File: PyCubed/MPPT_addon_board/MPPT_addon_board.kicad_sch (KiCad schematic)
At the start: 14 parts, among them J1 HW-09-08-L-D-285-SM-A, Q9 MBT2222ADW1T1, U1 LT8490-mezzanine, U2 LT8490-mezzanine

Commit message: adding version, name, and text on circuit board
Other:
- title: (none) -> MPPT addon board
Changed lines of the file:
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@@
 (kicad_sch (version 20230121) (generator eeschema)
   (paper "A4")
+  (title_block
+    (title "MPPT addon board")
+    (date "2024-05-07")
+    (rev "1.4")
+  )
   (junction (at 237.49 113.03) (diameter 0) (color 0 0 0 0)
   )

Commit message: finalized edits
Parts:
- added R29, R30: 10K, Resistor_SMD:R_0603_1608Metric, symbol Device:R_US
- C5, C6: value 0.1u -> 0.1uF
- U1, U2: value LT8490-mezzanine -> LT8491-mezzanine; footprint mainboard:LT8490-mezzanine -> mainboard:LT8491-mezzanine
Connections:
- net I2C Bus Protection/SDA_DEVICE: now also U1.12 (SDA); no longer U1.13 (SDA)
- net I2C Bus Protection/SDL_DEVICE: now also U1.13 (SCL); no longer U1.12 (SCL)
- net I2C Bus Protection1/SDA_DEVICE: now also U2.12 (SDA); no longer U2.13 (SDA)
- net I2C Bus Protection1/SDL_DEVICE: now also U2.13 (SCL); no longer U2.12 (SCL)
- net ~{SHDN_1}: now also R29.1; no longer Q9.5 (B2)
- net ~{SHDN_2}: now also R30.1; no longer Q9.2 (B1)
- new net: Q9.2 (B1), R30.2
- new net: Q9.5 (B2), R29.2
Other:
- note added: "Connector"
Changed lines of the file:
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@@
   (junction (at 92.71 41.91) (diameter 0) (color 0 0 0 0)
   )
+  (junction (at 224.79 58.42) (diameter 0) (color 0 0 0 0)
+  )
   (junction (at 118.11 139.7) (diameter 0) (color 0 0 0 0)
   )
@@
   (junction (at 118.11 129.54) (diameter 0) (color 0 0 0 0)
   )
+  (junction (at 207.01 128.27) (diameter 0) (color 0 0 0 0)
+  )
   (junction (at 92.71 72.39) (diameter 0) (color 0 0 0 0)
   )
@@
   )
   (junction (at 49.53 166.37) (diameter 0) (color 0 0 0 0)
+  )
+  (junction (at 238.76 58.42) (diameter 0) (color 0 0 0 0)
   )
   (no_connect (at 95.25 49.53))
@@
     (stroke (width 0) (type default))
   )
-  (wire (pts (xy 54.61 118.11) (xy 63.5 118.11))
+  (wire (pts (xy 45.72 118.11) (xy 55.88 118.11))
     (stroke (width 0) (type default))
   )
@@
     (stroke (width 0) (type default))
   )
+  (wire (pts (xy 44.45 57.15) (xy 58.42 57.15))
+    (stroke (width 0) (type default))
+  )
   (wire (pts (xy 115.57 111.76) (xy 129.54 111.76))
     (stroke (width 0) (type default))
@@
   )
   (wire (pts (xy 204.47 118.11) (xy 209.55 118.11))
-    (stroke (width 0) (type default))
-  )
-  (wire (pts (xy 55.88 57.15) (xy 66.04 57.15))
     (stroke (width 0) (type default))
   )
@@
     )
   )
+  (text "Connector\n" (at 214.63 95.25 0)
+    (effects (font (size 2.159 2.159)) (justify left bottom))
+  )
   (text "Local decoupling capasitors" (at 218.44 49.53 0)
     (effects (font (size 1.27 1.27)) (justify left bottom))
@@
     (effects (font (size 1.27 1.27)) (justify left bottom))
   )
-  (label "~{SHDN_1}" (at 55.88 57.15 0) (fields_autoplaced)
+  (label "~{SHDN_1}" (at 44.45 57.15 0) (fields_autoplaced)
     (effects (font (size 1.27 1.27)) (justify left bottom))
   )
@@
     (effects (font (size 1.27 1.27)) (justify right bottom))
   )
-  (label "~{SHDN_2}" (at 54.61 118.11 0) (fields_autoplaced)
+  (label "~{SHDN_2}" (at 45.72 118.11 0) (fields_autoplaced)
     (effects (font (size 1.27 1.27)) (justify left bottom))
   )
@@
     )
   )
+  (symbol (lib_id "power:PWR_FLAG") (at 207.01 128.27 90) (unit 1)
+    (in_bom yes) (on_board yes) (dnp no) (fields_autoplaced)
+    (property "Reference" "#FLG04" (at 205.105 128.27 0)
+      (effects (font (size 1.27 1.27)) hide)
+    )
+    (property "Value" "PWR_FLAG" (at 203.2 128.27 90)
+      (effects (font (size 1.27 1.27)) (justify left))
+    )
+    (property "Footprint" "" (at 207.01 128.27 0)
+      (effects (font (size 1.27 1.27)) hide)
+    )
+    (property "Datasheet" "~" (at 207.01 128.27 0)
+      (effects (font (size 1.27 1.27)) hide)
+    )
+    (pin "1")
+    (instances
+      (project "MPPT_addon_board"
+        (path "/280ad1e7-2eb5-41ea-be76-321f07a5cb3e"
+          (reference "#FLG04") (unit 1)
+        )
+      )
+    )
+  )
   (symbol (lib_id "Device:C") (at 224.79 64.77 0) (unit 1)
     (in_bom yes) (on_board yes) (dnp no) (fields_autoplaced)
@@
       (effects (font (size 1.27 1.27)) (justify left))
     )
-    (property "Value" "0.1u" (at 228.6 66.04 0)
+    (property "Value" "0.1uF" (at 228.6 66.04 0)
       (effects (font (size 1.27 1.27)) (justify left))
     )
@@
         (path "/280ad1e7-2eb5-41ea-be76-321f07a5cb3e"
           (reference "Q9") (unit 1)
+        )
+      )
+    )
+  )
+  (symbol (lib_id "power:PWR_FLAG") (at 238.76 58.42 270) (unit 1)
+    (in_bom yes) (on_board yes) (dnp no) (fields_autoplaced)
+    (property "Reference" "#FLG02" (at 240.665 58.42 0)
+      (effects (font (size 1.27 1.27)) hide)
+    )
+    (property "Value" "PWR_FLAG" (at 242.57 58.42 90)
+      (effects (font (size 1.27 1.27)) (justify left))
+    )
+    (property "Footprint" "" (at 238.76 58.42 0)
+      (effects (font (size 1.27 1.27)) hide)
+    )
+    (property "Datasheet" "~" (at 238.76 58.42 0)
+      (effects (font (size 1.27 1.27)) hide)
+    )
+    (pin "1")
+    (instances
+      (project "MPPT_addon_board"
+        (path "/280ad1e7-2eb5-41ea-be76-321f07a5cb3e"
+          (reference "#FLG02") (unit 1)
         )
       )
@@
       (effects (font (size 1.27 1.27)) (justify left))
     )
-    (property "Value" "0.1u" (at 242.57 66.04 0)
+    (property "Value" "0.1uF" (at 242.57 66.04 0)
       (effects (font (size 1.27 1.27)) (justify left))
     )
@@
       (effects (font (size 1.27 1.27)))
     )
-    (property "Value" "LT8490-mezzanine" (at 105.41 97.79 0)
-      (effects (font (size 1.27 1.27)))
-    )
-    (property "Footprint" "mainboard:LT8490-mezzanine" (at 100.33 97.79 0)
+    (property "Value" "LT8491-mezzanine" (at 105.41 97.79 0)
+      (effects (font (size 1.27 1.27)))
+    )
+    (property "Footprint" "mainboard:LT8491-mezzanine" (at 100.33 97.79 0)
       (effects (font (size 1.27 1.27)) hide)
     )
@@
     )
   )
+  (symbol (lib_id "power:PWR_FLAG") (at 224.79 58.42 90) (unit 1)
+    (in_bom yes) (on_board yes) (dnp no) (fields_autoplaced)
+    (property "Reference" "#FLG01" (at 222.885 58.42 0)
+      (effects (font (size 1.27 1.27)) hide)
+    )
+    (property "Value" "PWR_FLAG" (at 220.98 58.42 90)
+      (effects (font (size 1.27 1.27)) (justify left))
+    )
+    (property "Footprint" "" (at 224.79 58.42 0)
+      (effects (font (size 1.27 1.27)) hide)
+    )
+    (property "Datasheet" "~" (at 224.79 58.42 0)
+      (effects (font (size 1.27 1.27)) hide)
+    )
+    (pin "1")
+    (instances
+      (project "MPPT_addon_board"
+        (path "/280ad1e7-2eb5-41ea-be76-321f07a5cb3e"
+          (reference "#FLG01") (unit 1)
+        )
+      )
+    )
+  )
   (symbol (lib_id "power:GND") (at 92.71 142.24 0) (unit 1)
     (in_bom yes) (on_board yes) (dnp no) (fields_autoplaced)
@@
     )
   )
+  (symbol (lib_id "power:PWR_FLAG") (at 193.04 107.95 90) (unit 1)
+    (in_bom yes) (on_board yes) (dnp no) (fields_autoplaced)
+    (property "Reference" "#FLG03" (at 191.135 107.95 0)
+      (effects (font (size 1.27 1.27)) hide)
+    )
+    (property "Value" "PWR_FLAG" (at 189.23 107.95 90)
+      (effects (font (size 1.27 1.27)) (justify left))
+    )
+    (property "Footprint" "" (at 193.04 107.95 0)
+      (effects (font (size 1.27 1.27)) hide)
+    )
+    (property "Datasheet" "~" (at 193.04 107.95 0)
+      (effects (font (size 1.27 1.27)) hide)
+    )
+    (pin "1")
+    (instances
+      (project "MPPT_addon_board"
+        (path "/280ad1e7-2eb5-41ea-be76-321f07a5cb3e"
+          (reference "#FLG03") (unit 1)
+        )
+      )
+    )
+  )
+  (symbol (lib_id "Device:R_US") (at 59.69 118.11 90) (unit 1)
+    (in_bom yes) (on_board yes) (dnp no) (fields_autoplaced)
+    (property "Reference" "R30" (at 59.69 111.76 90)
+      (effects (font (size 1.27 1.27)))
+    )
+    (property "Value" "10K" (at 59.69 114.3 90)
+      (effects (font (size 1.27 1.27)))
+    )
+    (property "Footprint" "Resistor_SMD:R_0603_1608Metric" (at 59.944 117.094 90)
+      (effects (font (size 1.27 1.27)) hide)
+    )
+    (property "Datasheet" "~" (at 59.69 118.11 0)
+      (effects (font (size 1.27 1.27)) hide)
+    )
+    (property "note" "" (at 59.69 118.11 90)
+      (effects (font (size 1.27 1.27)) hide)
+    )
+    (pin "1")
+    (pin "2")
+    (instances
+      (project "MPPT_addon_board"
+        (path "/280ad1e7-2eb5-41ea-be76-321f07a5cb3e"
+          (reference "R30") (unit 1)
+        )
+      )
+    )
+  )
   (symbol (lib_id "power:GND") (at 238.76 71.12 0) (unit 1)
     (in_bom yes) (on_board yes) (dnp no) (fields_autoplaced)
@@
         (path "/280ad1e7-2eb5-41ea-be76-321f07a5cb3e"
           (reference "#PWR025") (unit 1)
+        )
+      )
+    )
+  )
+  (symbol (lib_id "Device:R_US") (at 62.23 57.15 90) (unit 1)
+    (in_bom yes) (on_board yes) (dnp no) (fields_autoplaced)
+    (property "Reference" "R29" (at 62.23 50.8 90)
+      (effects (font (size 1.27 1.27)))
+    )
+    (property "Value" "10K" (at 62.23 53.34 90)
+      (effects (font (size 1.27 1.27)))
+    )
+    (property "Footprint" "Resistor_SMD:R_0603_1608Metric" (at 62.484 56.134 90)
+      (effects (font (size 1.27 1.27)) hide)
+    )
+    (property "Datasheet" "~" (at 62.23 57.15 0)
+      (effects (font (size 1.27 1.27)) hide)
+    )
+    (property "note" "" (at 62.23 57.15 90)
+      (effects (font (size 1.27 1.27)) hide)
+    )
+    (pin "1")
+    (pin "2")
+    (instances
+      (project "MPPT_addon_board"
+        (path "/280ad1e7-2eb5-41ea-be76-321f07a5cb3e"
+          (reference "R29") (unit 1)
         )
       )
@@
         (path "/280ad1e7-2eb5-41ea-be76-321f07a5cb3e"
           (reference "#PWR024") (unit 1)
+        )
+      )
+    )
+  )
+  (symbol (lib_id "power:PWR_FLAG") (at 193.04 123.19 90) (unit 1)
+    (in_bom yes) (on_board yes) (dnp no) (fields_autoplaced)
+    (property "Reference" "#FLG05" (at 191.135 123.19 0)
+      (effects (font (size 1.27 1.27)) hide)
+    )
+    (property "Value" "PWR_FLAG" (at 189.23 123.19 90)
+      (effects (font (size 1.27 1.27)) (justify left))
+    )
+    (property "Footprint" "" (at 193.04 123.19 0)
+      (effects (font (size 1.27 1.27)) hide)
+    )
+    (property "Datasheet" "~" (at 193.04 123.19 0)
+      (effects (font (size 1.27 1.27)) hide)
+    )
+    (pin "1")
+    (instances
+      (project "MPPT_addon_board"
+        (path "/280ad1e7-2eb5-41ea-be76-321f07a5cb3e"
+          (reference "#FLG05") (unit 1)
         )
       )
@@
       (effects (font (size 1.27 1.27)))
     )
-    (property "Value" "LT8490-mezzanine" (at 105.41 38.1 0)
-      (effects (font (size 1.27 1.27)))
-    )
-    (property "Footprint" "mainboard:LT8490-mezzanine" (at 100.33 38.1 0)
-      (effects (font (size 1.27 1.27)) hide)
-    )
+    (property "Value" "LT8491-mezzanine" (at 105.41 38.1 0)
+      (effects (font (size 1.27 1.27)))
+    )
+    (property "Footprint" "mainboard:LT8491-mezzanine" (at 100.33 38.1 0)
+      (effects (font (size 1.27 1.27)) hide)
+    )

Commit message: cleaned up, added gerbers
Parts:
- H1, H2, H3, H4: now left out of the parts list
- J1: footprint HW_09_08_L_D_285_SM_A(1):SAMTEC_HW-09-XX-X-D-XXX-SM-A -> mainboard:SAMTEC_HW-09-XX-X-D-XXX-SM-A; symbol HW-09-XX-X-D-XXX-SM-A:HW-09-XX-X-D-XXX-SM-A -> mainboard:HW-09-08-L-D-285-SM-A
- R15, R2: now not fitted; now left out of the parts list
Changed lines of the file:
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@@
   (title_block
     (title "MPPT addon board")
-    (date "2024-05-07")
+    (date "2024-05-08")
     (rev "1.4")
   )
@@
   )
   (symbol (lib_id "Device:R_US") (at 129.54 105.41 0) (unit 1)
-    (in_bom yes) (on_board yes) (dnp no) (fields_autoplaced)
+    (in_bom no) (on_board yes) (dnp yes) (fields_autoplaced)
     (property "Reference" "R15" (at 132.08 104.14 0)
       (effects (font (size 1.27 1.27)) (justify left))
@@
   )
   (symbol (lib_id "Mechanical:MountingHole_Pad") (at 46.99 166.37 90) (unit 1)
-    (in_bom yes) (on_board yes) (dnp no)
+    (in_bom no) (on_board yes) (dnp no)
     (property "Reference" "H4" (at 40.64 166.37 90)
       (effects (font (size 1.27 1.27)))
@@
   )
   (symbol (lib_id "Mechanical:MountingHole_Pad") (at 46.99 158.75 90) (unit 1)
-    (in_bom yes) (on_board yes) (dnp no)
+    (in_bom no) (on_board yes) (dnp no)
     (property "Reference" "H2" (at 40.64 158.75 90)
       (effects (font (size 1.27 1.27)))
@@
     )
   )
-  (symbol (lib_id "HW-09-XX-X-D-XXX-SM-A:HW-09-XX-X-D-XXX-SM-A") (at 222.25 115.57 0) (unit 1)
+  (symbol (lib_id "mainboard:HW-09-08-L-D-285-SM-A") (at 222.25 115.57 0) (unit 1)
     (in_bom yes) (on_board yes) (dnp no)
     (property "Reference" "J1" (at 222.25 97.79 0)
@@
       (effects (font (size 1.27 1.27)))
     )
-    (property "Footprint" "HW_09_08_L_D_285_SM_A(1):SAMTEC_HW-09-XX-X-D-XXX-SM-A" (at 222.25 115.57 0)
+    (property "Footprint" "mainboard:SAMTEC_HW-09-XX-X-D-XXX-SM-A" (at 222.25 115.57 0)
       (effects (font (size 1.27 1.27)) (justify bottom) hide)
     )
@@
   )
   (symbol (lib_id "Mechanical:MountingHole_Pad") (at 46.99 162.56 90) (unit 1)
-    (in_bom yes) (on_board yes) (dnp no)
+    (in_bom no) (on_board yes) (dnp no)
     (property "Reference" "H3" (at 40.64 162.56 90)
       (effects (font (size 1.27 1.27)))
@@
   )
   (symbol (lib_id "Device:R_US") (at 140.97 52.07 90) (unit 1)
-    (in_bom yes) (on_board yes) (dnp no) (fields_autoplaced)
+    (in_bom no) (on_board yes) (dnp yes) (fields_autoplaced)
     (property "Reference" "R2" (at 140.97 45.72 90)
       (effects (font (size 1.27 1.27)))
@@
   )
   (symbol (lib_id "Mechanical:MountingHole_Pad") (at 46.99 154.94 90) (unit 1)
-    (in_bom yes) (on_board yes) (dnp no)
+    (in_bom no) (on_board yes) (dnp no)
     (property "Reference" "H1" (at 40.64 154.94 90)
       (effects (font (size 1.27 1.27)))

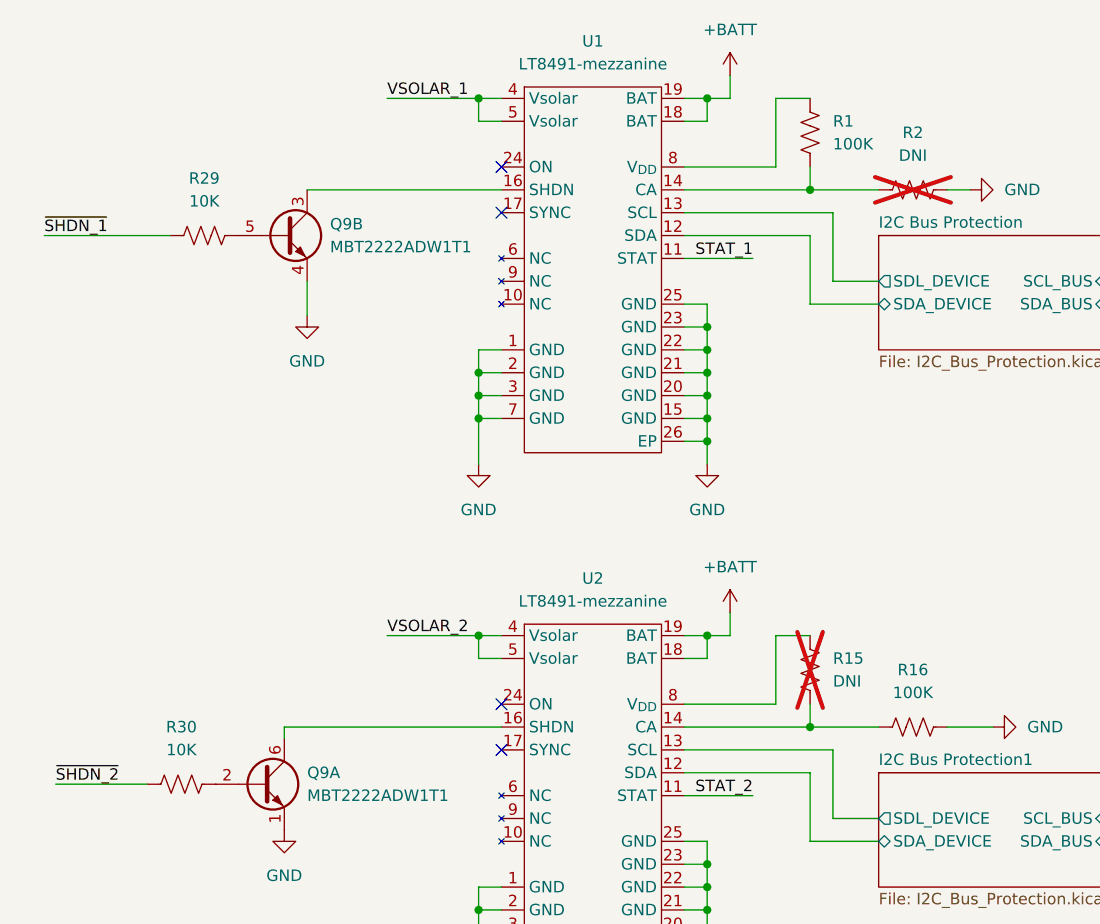
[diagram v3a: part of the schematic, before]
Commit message: cleaned up BOM, added connector numbers for Pycubed; cleaned up MPPT add-on BOM
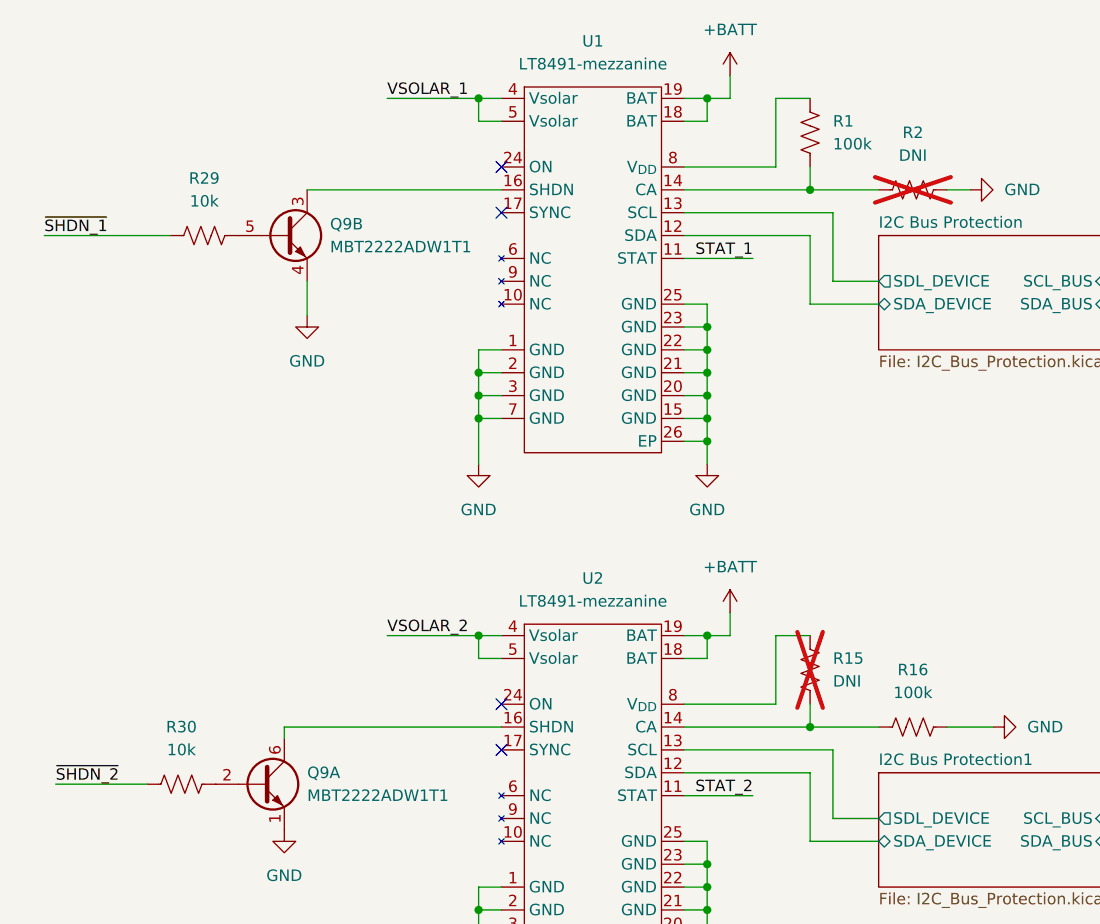
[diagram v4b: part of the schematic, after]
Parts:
- R1, R16: value 100K -> 100k
- R29, R30: value 10K -> 10k
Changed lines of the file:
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@@
       (effects (font (size 1.27 1.27)))
     )
-    (property "Value" "100K" (at 140.97 107.95 90)
+    (property "Value" "100k" (at 140.97 107.95 90)
       (effects (font (size 1.27 1.27)))
     )
@@
       (effects (font (size 1.27 1.27)))
     )
-    (property "Value" "10K" (at 59.69 114.3 90)
+    (property "Value" "10k" (at 59.69 114.3 90)
       (effects (font (size 1.27 1.27)))
     )
@@
       (effects (font (size 1.27 1.27)))
     )
-    (property "Value" "10K" (at 62.23 53.34 90)
+    (property "Value" "10k" (at 62.23 53.34 90)
       (effects (font (size 1.27 1.27)))
     )
@@
       (effects (font (size 1.27 1.27)) (justify left))
     )
-    (property "Value" "100K" (at 132.08 46.99 0)
-      (effects (font (size 1.27 1.27)) (justify left))
-    )
+    (property "Value" "100k" (at 132.08 46.99 0)
+      (effects (font (size 1.27 1.27)) (justify left))
+    )

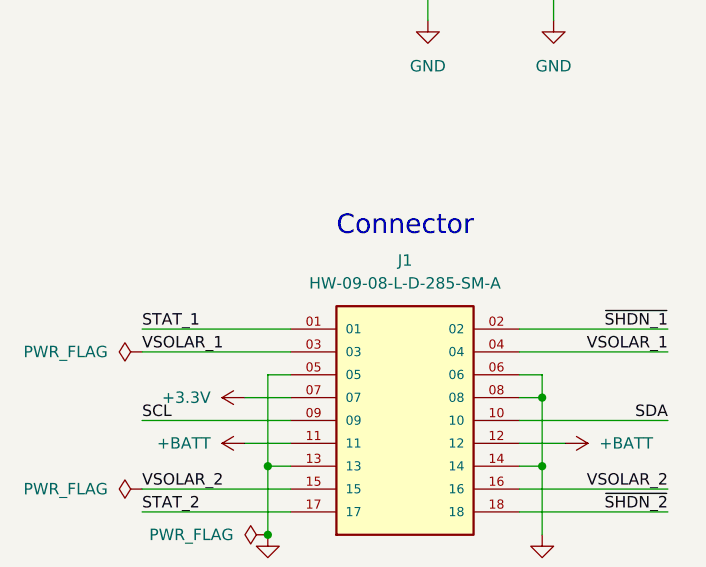
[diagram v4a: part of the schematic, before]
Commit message: Updated component values, iBOM, and schematic printouts
Pycubed:
+ LT3652 MPP and Imax changes: R10 (MPPT to 20k), R19 (Rsense to 0.27), R16 from 50k to 49.9k
+ Neopixel to 1655
+ SAMD from AU to AF (better temp rating)

MPPT add-on:
+ connector to HW-09-10-L-D-400-SM
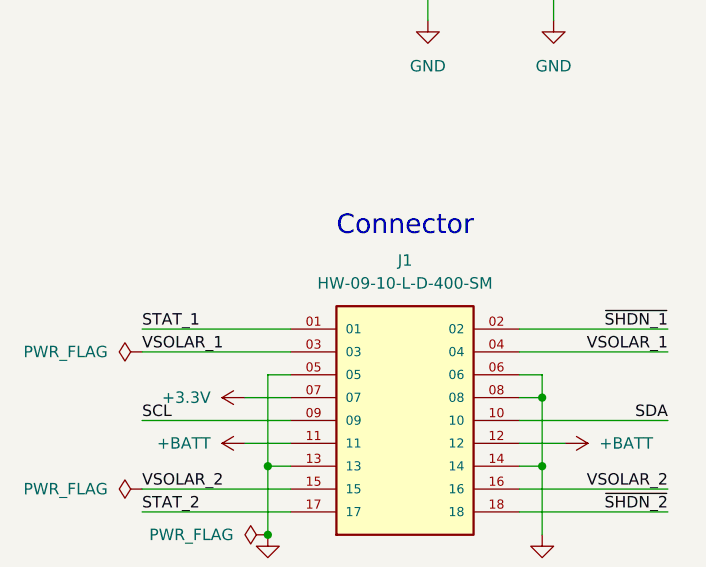
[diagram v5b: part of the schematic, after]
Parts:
- J1: value HW-09-08-L-D-285-SM-A -> HW-09-10-L-D-400-SM; symbol mainboard:HW-09-08-L-D-285-SM-A -> mainboard:HW-09-10-L-D-400-SM
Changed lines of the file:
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@@
     )
   )
-  (symbol (lib_id "mainboard:HW-09-08-L-D-285-SM-A") (at 222.25 115.57 0) (unit 1)
+  (symbol (lib_id "mainboard:HW-09-10-L-D-400-SM") (at 222.25 115.57 0) (unit 1)
     (in_bom yes) (on_board yes) (dnp no)
     (property "Reference" "J1" (at 222.25 97.79 0)
       (effects (font (size 1.27 1.27)))
     )
-    (property "Value" "HW-09-08-L-D-285-SM-A" (at 222.25 100.33 0)
+    (property "Value" "HW-09-10-L-D-400-SM" (at 222.25 100.33 0)
       (effects (font (size 1.27 1.27)))
     )
